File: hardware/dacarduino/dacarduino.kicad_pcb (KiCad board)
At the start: 2 copper layers, 100 x 95 mm, 84 parts, among them J1 Conn_01x03_Male, J10 GATE IN, J11 CV IN, J12 CV IN, J13 CV IN, J14 CV IN, J15 CV IN, J16 CV IN, J17 VCC, J18 Vin, J19 EURO_PWR_2x5, J2 Conn_01x03_Male, J3 CV OUT A, J4 CV OUT B, J5 GATE OUT A, J6 GATE OUT B, J7 GATE IN, J8 GATE IN, J9 GATE IN, Q1 2N3904, Q2 2N3904, Q3 2N3904, Q4 2N3904, Q5 2N3904, Q6 2N3904, U1 MCP4922, U2 TL972

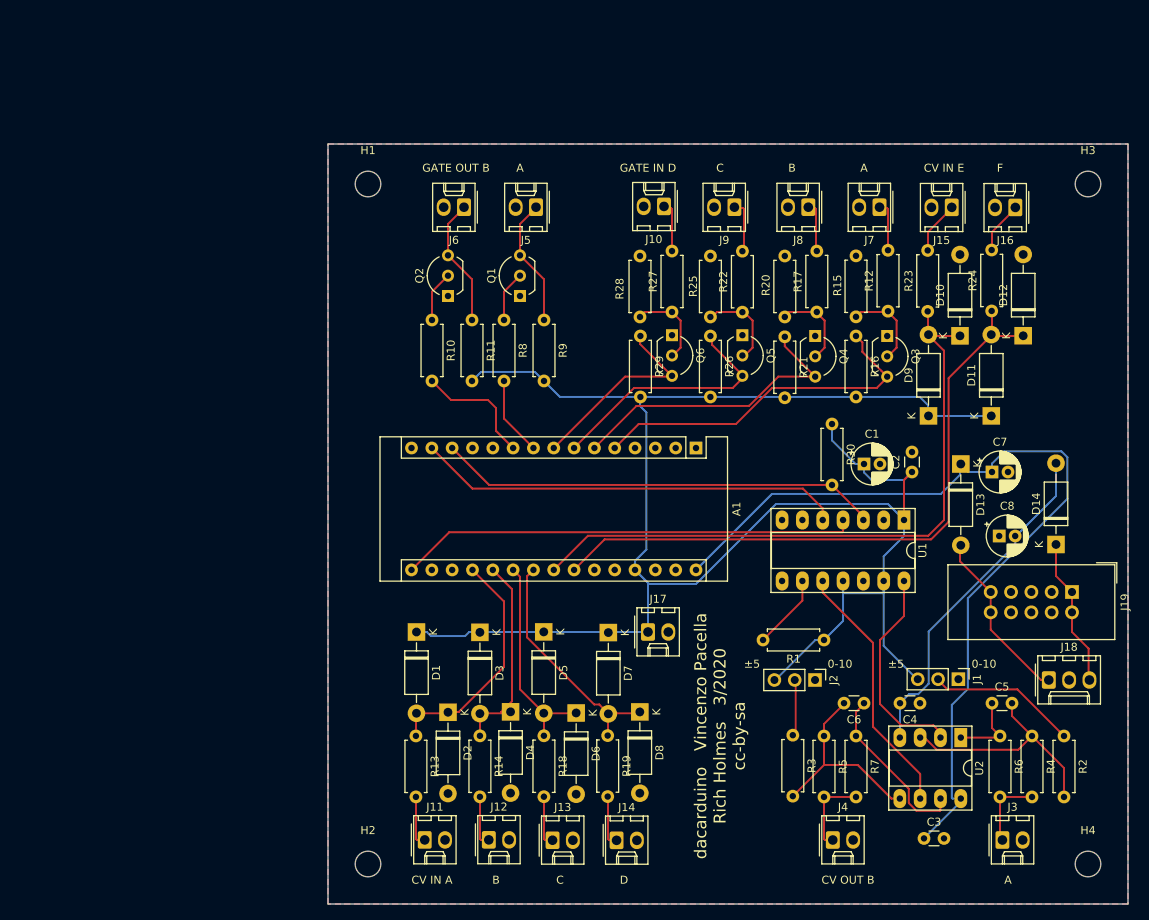
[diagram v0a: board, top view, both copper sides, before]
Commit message: Revised layout, with voltage reference restored to dacarduino
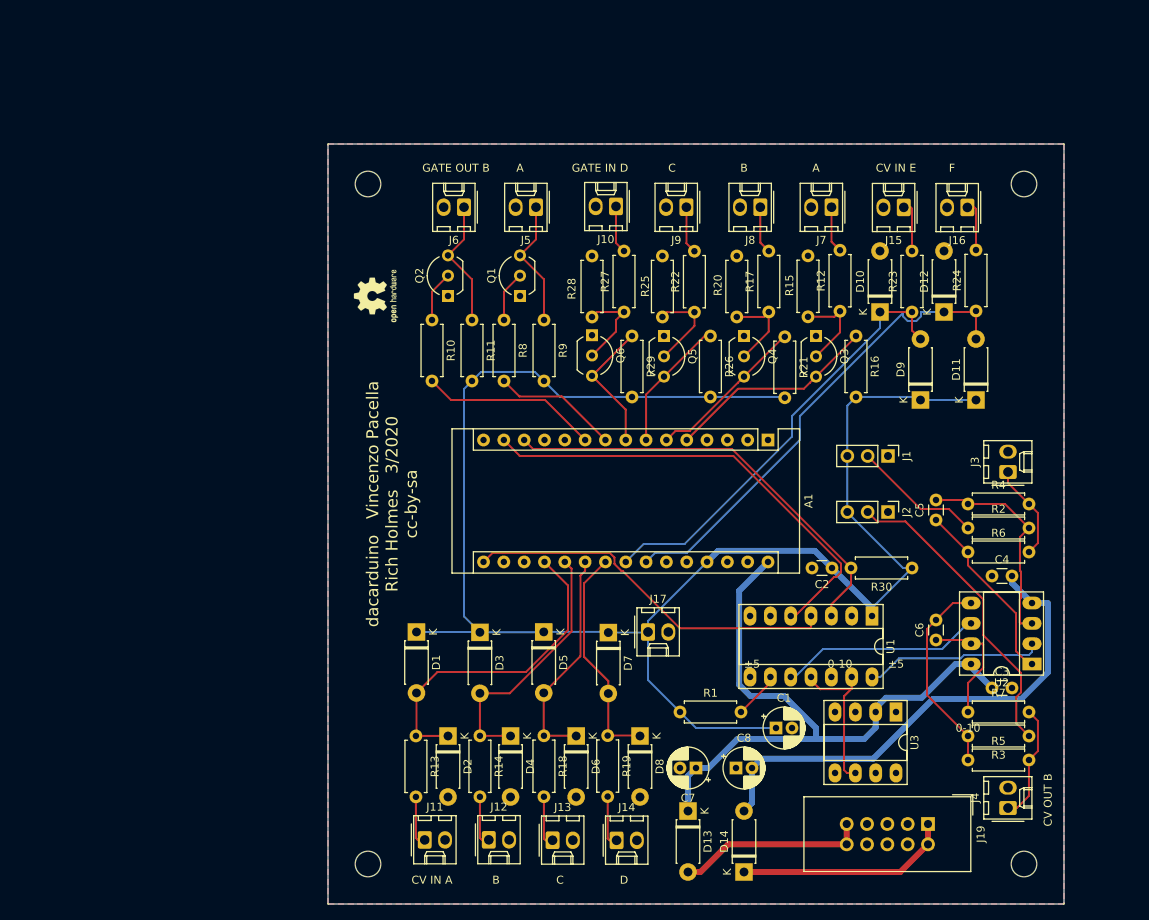
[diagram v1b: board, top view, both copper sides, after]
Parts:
- removed J18: Vin, Connector_Molex:Molex_KK-254_AE-6410-03A_1x03_P2.54mm_Vertical
- added REF**: OSHW-Logo2_7.3x6mm_SilkScreen, Symbol:OSHW-Logo2_7.3x6mm_SilkScreen, F.Cu at (131.0, 79.0)
- added U3: REF02CP+, Package_DIP:DIP-8_W7.62mm_Socket_LongPads, F.Cu at (196.0, 131.0)
- D1, D10, D11, D12, D13, D14, D2, D3, D4, D5, D6, D7, D8, D9: footprint Diode_THT:D_DO-41_SOD81_P10.16mm_Horizontal -> Diode_THT:D_DO-41_SOD81_P7.62mm_Horizontal
- moved D14 56.5 mm to (177.0, 151.0)
- moved D13 55.2 mm to (170.0, 143.4)
- moved C7 52.3 mm to (171.0, 138.0), turned to 180 degrees
- moved J3 46.0 mm to (210.0, 101.0), turned to 90 degrees
- moved C8 43.9 mm to (176.0, 138.0)
- moved C1 34.8 mm to (181.0, 133.0)
- moved J19 34.1 mm to (200.0, 145.0)
- moved R4 30.1 mm to (205.0, 105.0), turned to 0 degrees
- moved R3 29.5 mm to (212.6, 134.0), turned to 180 degrees
- moved J1 29.3 mm to (195.0, 99.0)
- moved R2 28.6 mm to (205.0, 108.0), turned to 0 degrees
- moved C5 23.9 mm to (201.0, 107.0), turned to 90 degrees
- moved R6 23.3 mm to (205.0, 111.0), turned to 0 degrees
- moved J2 22.9 mm to (195.0, 106.0)
- moved J4 22.3 mm to (210.0, 143.0), turned to 90 degrees
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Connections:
- net CV_OUT_A renamed /CV out/CV_OUT_A
- net CV_OUT_B renamed /CV out/CV_OUT_B
- net GATE_OUT_A renamed /Gate out/GATE_OUT_A
- net GATE_OUT_B renamed /Gate out/GATE_OUT_B
- U1 pad 11: VCC -> /Voltage reference/VREF
- U1 pad 13: VCC -> /Voltage reference/VREF
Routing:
- net Net-(J2-Pad2): track 7.19 -> 38.9 mm
- net +12V: track 111.7 -> 81.0 mm
- net /Arduino/A_IN_E: track 82.3 -> 55.2 mm
- net VCC: track 237.2 -> 212.1 mm
- net /Arduino/A_IN_F: track 81.8 -> 60.9 mm
- net -12V: track 43.0 -> 63.2 mm
- net /Voltage reference/VREF: track 0.00 -> 19.6 mm
- net /Arduino/D_IN_A: track 44.6 -> 26.6 mm
- net /Arduino/D_IN_B: track 37.9 -> 20.1 mm
- net /Arduino/D_IN_C: track 31.7 -> 16.8 mm
- net Net-(C5-Pad1): track 9.40 -> 23.2 mm
- net /Arduino/A_IN_A: track 30.0 -> 41.3 mm
- net /Arduino/SCK: track 57.4 -> 47.2 mm
- net Net-(D14-Pad1): track 18.7 -> 27.0 mm
- net /Arduino/D_IN_D: track 25.0 -> 16.8 mm
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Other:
- board size 100 x 95 mm -> 92 x 95 mm

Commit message: Backlog of many changes
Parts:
- removed D10, D11, D12, D5, D6, D7, D8, D9: 1N5817, Diode_THT:D_DO-41_SOD81_P7.62mm_Horizontal
- removed J13, J14, J15, J16: CV IN, Connector_Molex:Molex_KK-254_AE-6410-02A_1x02_P2.54mm_Vertical
- removed R18, R19, R23, R24: 1k, Resistor_THT:R_Axial_DIN0207_L6.3mm_D2.5mm_P7.62mm_Horizontal
- removed REF**: OSHW-Logo2_7.3x6mm_SilkScreen, Symbol:OSHW-Logo2_7.3x6mm_SilkScreen
- added J501: Conn_01x04, Connector_Wire:SolderWirePad_1x04_P3.81mm_Drill1.2mm, F.Cu at (159.0, 117.0)
- J303: renamed from J3; value CV OUT A -> Molex 2 pin
- J304: renamed from J4; value CV OUT B -> Molex 2 pin
- J401: renamed from J5; value GATE OUT A -> Molex 2 pin
- J402: renamed from J6; value GATE OUT B -> Molex 2 pin
- U301: renamed from U2; value TL972 -> TL072
- moved J301 21.5 mm to (212.5, 86.5)
- moved J302 21.5 mm to (212.5, 93.5)
- moved H101 10.0 mm to (140.0, 65.0)
- moved H102 10.0 mm to (140.0, 150.0)
- moved D1001 9.00 mm to (145.1, 121.0)
- moved D1002 9.00 mm to (149.0, 134.0)
- moved D1101 9.00 mm to (153.0, 121.0)
- moved D1102 9.00 mm to (156.8, 134.0)
- moved J1001 9.00 mm to (146.1, 147.0)
- moved J1101 9.00 mm to (154.1, 147.0)
- moved R1001 9.00 mm to (145.0, 134.0)
- moved R1101 9.00 mm to (153.0, 134.0)
- moved A1201 8.06 mm to (188.0, 96.0)
- moved C202 8.06 mm to (196.0, 112.0)
- moved J401 8.06 mm to (159.0, 66.9)
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- renumbered A1 to A1201, C7 to C1301, C8 to C1302, C1 to C201, C2 to C202, C3 to C301, C4 to C302, C5 to C303, C6 to C304, D1 to D1001, D2 to D1002, D3 to D1101, D4 to D1102, D13 to D1301, D14 to D1302, H1 to H101, H2 to H102, H3 to H103, H4 to H104, J11 to J1001, J12 to J1101, J17 to J1201, J19 to J1301, J1 to J301, J2 to J302, J7 to J601, J8 to J701, J9 to J801, J10 to J901, Q1 to Q401, Q2 to Q402, Q3 to Q601, Q4 to Q701, Q5 to Q801, Q6 to Q901, R13 to R1001, R14 to R1101, R30 to R1201, R1 to R201, R2 to R301, R3 to R302, R4 to R303, R5 to R304, R6 to R305, R7 to R306, R8 to R401, R9 to R402, R10 to R403, R11 to R404, R12 to R601, R15 to R602, R16 to R603, R17 to R701, R20 to R702, R21 to R703, R22 to R801, R25 to R802, R26 to R803, R27 to R901, R28 to R902, R29 to R903, U3 to U1401, U1 to U201
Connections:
- net +12V renamed +VIN
- net -12V renamed -VIN
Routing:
- net /Arduino/A_IN_F: track 60.9 -> 6.73 mm
- net /Arduino/A_IN_E: track 55.2 -> 7.25 mm
- net VCC: track 212.1 -> 188.0 mm
- net /Arduino/A_IN_D: track 28.2 -> 7.78 mm
- net /Arduino/A_IN_C: track 27.9 -> 8.53 mm
- net Net-(J301-Pad2): track 16.3 -> 29.2 mm
- net /Arduino/MOSI: track 59.0 -> 49.1 mm
- net /Arduino/DAC_CS: track 54.5 -> 44.8 mm
- net /Arduino/SCK: track 47.2 -> 38.6 mm
- net /Arduino/A_IN_A: track 41.3 -> 33.0 mm
- net +VIN: track 81.0 -> 74.3 mm
- net /Inputs/CV in D/CV_IN: track 6.44 -> 0.00 mm
- net /Inputs/CV in C/CV_IN: track 6.40 -> 0.00 mm
- net /Inputs/CV in E/CV_IN: track 6.40 -> 0.00 mm
- net /Inputs/CV in F/CV_IN: track 6.28 -> 0.00 mm
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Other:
- board size 92 x 95 mm -> 82 x 95 mm
- board text added: "A_C A_D A_E A_F"
- board text added: "CV OUT A"
- board text removed: "CV IN E"
- board text removed: "D"
- board text removed: "F"

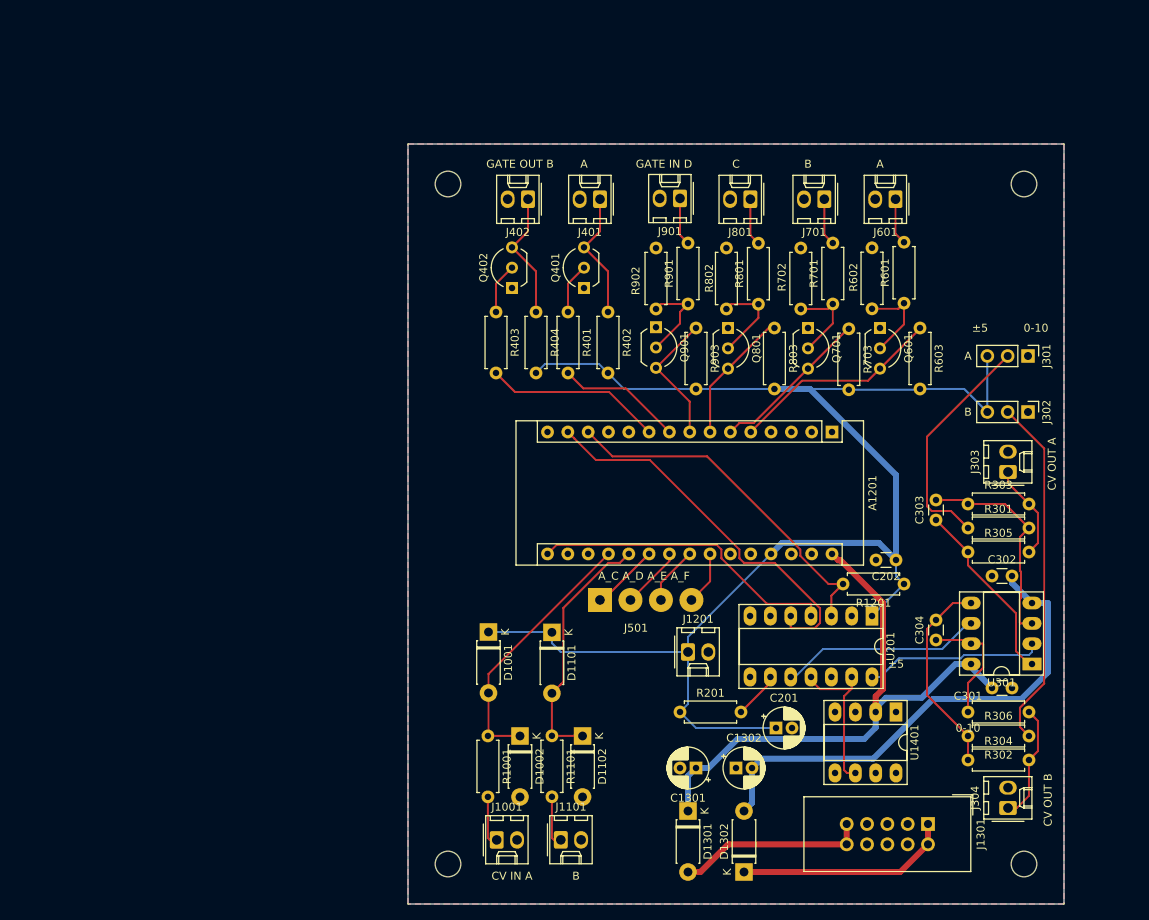
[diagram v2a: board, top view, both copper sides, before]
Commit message: Redid layout completely
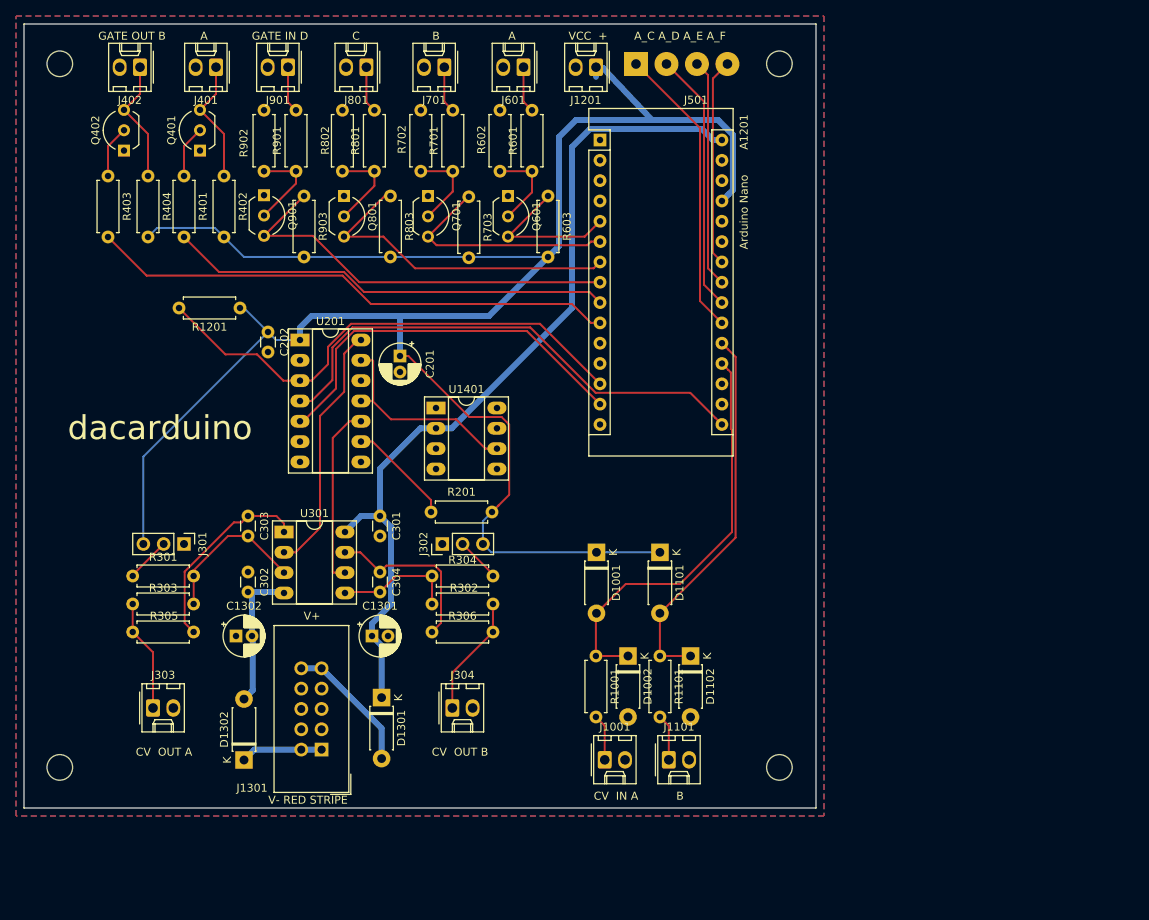
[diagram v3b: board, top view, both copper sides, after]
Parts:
- moved J303 110.9 mm to (103.1, 130.5), turned to 0 degrees
- moved J301 108.1 mm to (107.0, 110.0)
- moved R301 104.6 mm to (100.6, 114.0)
- moved R303 97.6 mm to (108.2, 117.5), turned to 180 degrees
- moved R305 97.3 mm to (108.2, 121.0), turned to 180 degrees
- moved U301 94.9 mm to (119.5, 108.5), turned to 0 degrees
- moved C302 93.0 mm to (115.0, 113.5), turned to 270 degrees
- moved R1201 89.9 mm to (114.0, 80.5)
- moved C303 86.0 mm to (115.0, 106.5), turned to 270 degrees
- moved C202 83.5 mm to (117.5, 83.5), turned to 270 degrees
- moved C301 79.5 mm to (131.5, 106.5), turned to 270 degrees
- moved U201 79.4 mm to (121.5, 84.5), turned to 0 degrees
- moved J1301 76.4 mm to (124.2, 135.7), turned to 180 degrees
- moved J302 75.1 mm to (139.3, 110.0), turned to 90 degrees
- moved J1201 74.0 mm to (158.5, 50.4), turned to 180 degrees
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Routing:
- net VCC: track 188.0 -> 250.2 mm
- net -VIN: track 63.2 -> 18.6 mm
- net /Arduino/D_OUT_B: track 22.2 -> 65.9 mm
- net /Arduino/D_OUT_A: track 15.7 -> 55.4 mm
- net Net-(J302-Pad2): track 44.1 -> 5.57 mm
- net /Arduino/D_IN_D: track 16.8 -> 51.5 mm
- net +VIN: track 74.3 -> 108.6 mm
- net /Arduino/A_IN_C: track 8.53 -> 36.8 mm
- net /Arduino/SCK: track 38.6 -> 64.0 mm
- net /Arduino/D_IN_C: track 16.8 -> 41.9 mm
- net /Arduino/A_IN_D: track 7.78 -> 32.7 mm
- net Net-(J301-Pad2): track 29.2 -> 5.61 mm
- net /Arduino/A_IN_E: track 7.25 -> 28.6 mm
- net /Arduino/A_IN_F: track 6.73 -> 26.0 mm
- net /Arduino/A_IN_A: track 33.0 -> 52.1 mm
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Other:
- board size 82 x 95 mm -> 99 x 98 mm
- board text added: "Arduino Nano"
- board text added: "V+"
- board text added: "V- RED STRIPE"
- board text added: "VCC +"
- board text added: "dacarduino"
- board text removed: "0-10"
- board text removed: "±5"

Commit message: Additional inputs since the board has room
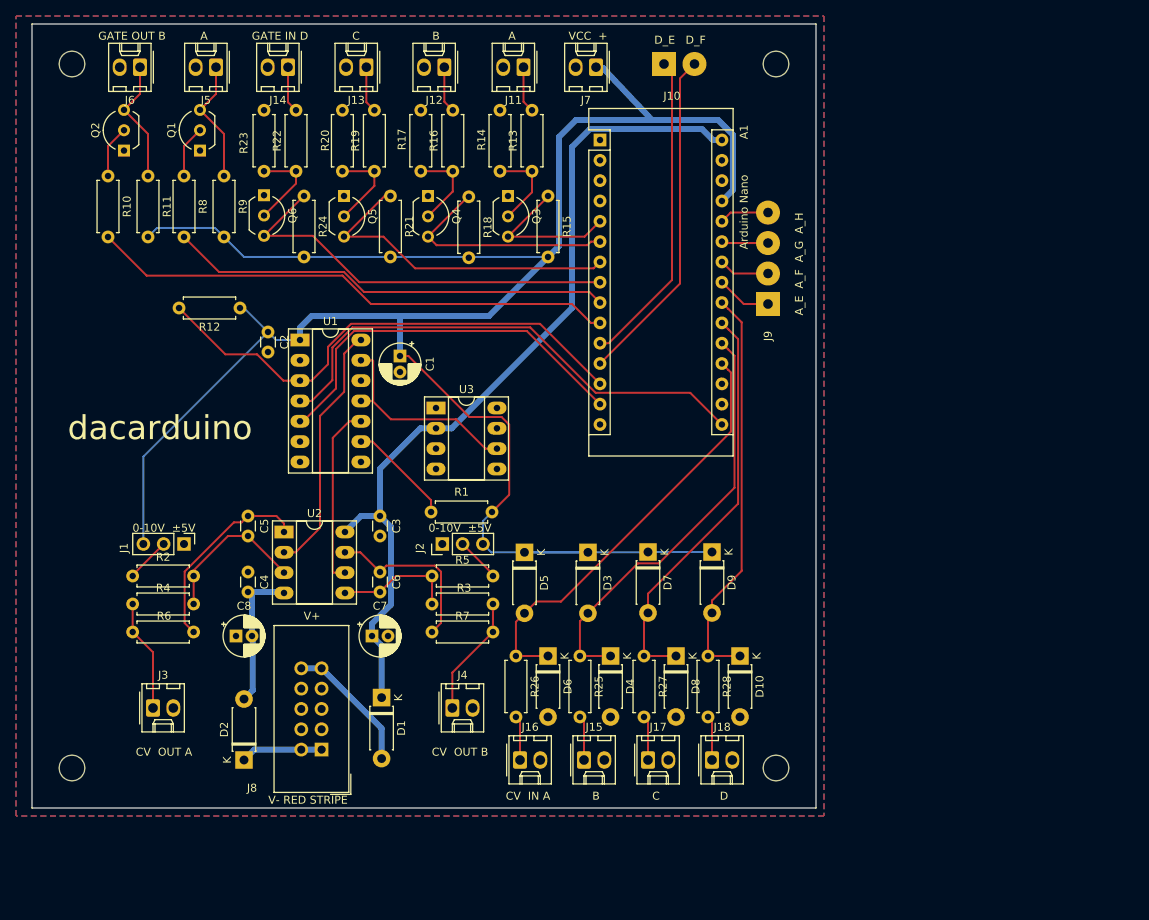
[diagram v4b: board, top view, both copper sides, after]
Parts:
- added D10: 1N5817, Diode_THT:D_DO-41_SOD81_P7.62mm_Horizontal, F.Cu at (176.5, 124.0)
- added D7: 1N5817, Diode_THT:D_DO-41_SOD81_P7.62mm_Horizontal, F.Cu at (165.0, 111.0)
- added D8: 1N5817, Diode_THT:D_DO-41_SOD81_P7.62mm_Horizontal, F.Cu at (168.5, 124.0)
- added D9: 1N5817, Diode_THT:D_DO-41_SOD81_P7.62mm_Horizontal, F.Cu at (173.0, 111.0)
- added J10: Conn_01x02, Connector_Wire:SolderWirePad_1x02_P3.81mm_Drill1.2mm, F.Cu at (167.0, 50.0)
- added J17: CV IN, Connector_Molex:Molex_KK-254_AE-6410-02A_1x02_P2.54mm_Vertical, F.Cu at (165.0, 137.0)
- added J18: CV IN, Connector_Molex:Molex_KK-254_AE-6410-02A_1x02_P2.54mm_Vertical, F.Cu at (173.0, 137.0)
- added R27: 1k, Resistor_THT:R_Axial_DIN0207_L6.3mm_D2.5mm_P7.62mm_Horizontal, F.Cu at (164.5, 124.0)
- added R28: 1k, Resistor_THT:R_Axial_DIN0207_L6.3mm_D2.5mm_P7.62mm_Horizontal, F.Cu at (172.5, 124.0)
- moved J9 34.2 mm to (180.0, 80.0), turned to 90 degrees
- moved J15 10.6 mm to (157.0, 137.0)
- moved J16 10.6 mm to (149.0, 137.0)
- moved D4 10.0 mm to (160.3, 124.0)
- moved D6 10.0 mm to (152.5, 124.0)
- moved R25 10.0 mm to (156.5, 124.0)
- moved R26 10.0 mm to (148.5, 124.0)
- moved D3 9.00 mm to (157.5, 111.0)
- moved D5 9.00 mm to (149.6, 111.0)
- moved H2 1.53 mm to (93.0, 138.0)
- moved H1 1.53 mm to (93.0, 50.0)
- moved H4 0.43 mm to (181.0, 138.0)
- moved H3 0.43 mm to (181.0, 50.0)
- renumbered A1201 to A1, C201 to C1, C202 to C2, C301 to C3, C302 to C4, C303 to C5, C304 to C6, C1301 to C7, C1302 to C8, D1301 to D1, D1302 to D2, D1101 to D3, D1102 to D4, D1001 to D5, D1002 to D6, H101 to H1, H102 to H2, H103 to H3, H104 to H4, J301 to J1, J601 to J11, J701 to J12, J801 to J13, J901 to J14, J1101 to J15, J1001 to J16, J302 to J2, J303 to J3, J304 to J4, J401 to J5, J402 to J6, J1201 to J7, J1301 to J8, J501 to J9, Q401 to Q1, Q402 to Q2, Q601 to Q3, Q701 to Q4, Q801 to Q5, Q901 to Q6, R201 to R1, R403 to R10, R404 to R11, R1201 to R12, R601 to R13, R602 to R14, R603 to R15, R701 to R16, R702 to R17, R703 to R18, R801 to R19, R301 to R2, R802 to R20, R803 to R21, R901 to R22, R902 to R23, R903 to R24, R1101 to R25, R1001 to R26, R302 to R3, R303 to R4, R304 to R5, R305 to R6, R306 to R7, R401 to R8, R402 to R9, U201 to U1, U301 to U2, U1401 to U3
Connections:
- A1 pad 11: Net-(A1201-Pad11) -> /Arduino/D_IN_E
- A1 pad 12: Net-(A1201-Pad12) -> /Arduino/D_IN_F
- A1 pad 25: Net-(A1201-Pad25) -> /Arduino/A_IN_G
- A1 pad 26: Net-(A1201-Pad26) -> /Arduino/A_IN_H
- J9 pad 1: /Arduino/A_IN_C -> /Arduino/A_IN_E
- J9 pad 2: /Arduino/A_IN_D -> /Arduino/A_IN_F
- J9 pad 3: /Arduino/A_IN_E -> /Arduino/A_IN_G
- J9 pad 4: /Arduino/A_IN_F -> /Arduino/A_IN_H
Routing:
- net /Arduino/D_IN_F: track 0.00 -> 42.3 mm
- net /Arduino/D_IN_E: track 0.00 -> 39.7 mm
- net /Arduino/A_IN_E: track 28.6 -> 6.89 mm
- net /Arduino/A_IN_F: track 26.0 -> 6.60 mm
- net /Arduino/A_IN_D: track 32.7 -> 51.0 mm
- net /Arduino/A_IN_C: track 36.8 -> 51.4 mm
- net VCC: track 250.2 -> 264.7 mm
- net /Arduino/A_IN_H: track 0.00 -> 6.21 mm
- net /Arduino/A_IN_G: track 0.00 -> 5.83 mm
- net /Inputs/CV in C/CV_IN: track 0.00 -> 5.59 mm
- net /Inputs/CV IN D/CV_IN: track 0.00 -> 5.59 mm
- net /Arduino/A_IN_B: track 47.6 -> 53.1 mm
- net /Arduino/A_IN_A: track 52.1 -> 54.0 mm
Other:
- board size 99 x 98 mm -> 98 x 98 mm
- board text added: "0-10V ±5V"
- board text added: "A_E A_F A_G A_H"
- board text added: "D"
- board text added: "D_E D_F"
- board text removed: "A_C A_D A_E A_F"
